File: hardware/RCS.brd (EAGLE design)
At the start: 47 x 40.5 mm, 60 parts, among them U1 LT1930, U2 TD62083AFNG, U3 HX711, U4 HX711

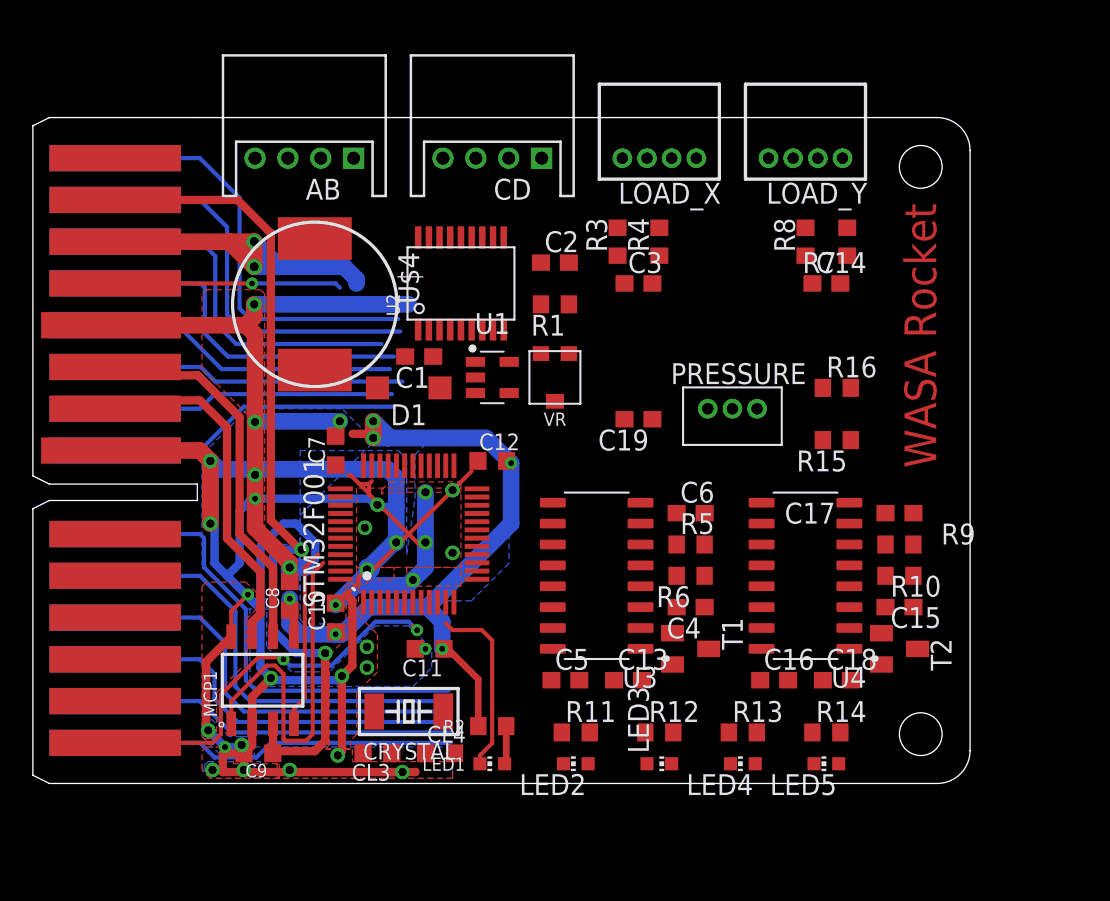
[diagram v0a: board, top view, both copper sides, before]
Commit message: RCS基板を追加
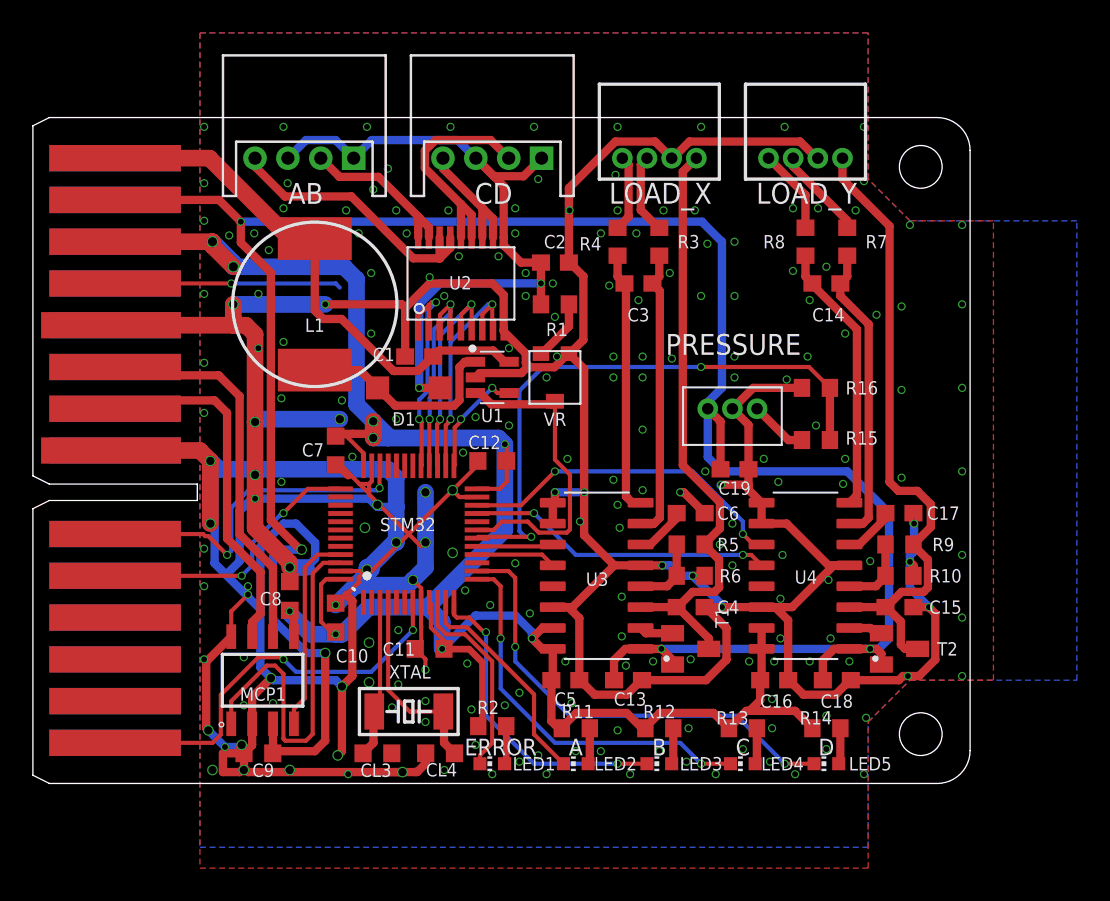
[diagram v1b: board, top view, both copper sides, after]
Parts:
- moved C19 6.59 mm to (42.7, 19.2), turned to 0 degrees
- moved R3 2.54 mm to (38.1, 33.0)
- moved R4 2.54 mm to (35.6, 33.0)
- moved R15 1.27 mm to (47.6, 21.0)
- moved R16 1.27 mm to (47.6, 24.1)
- moved R11 0.25 mm to (33.0, 3.43)
- moved R12 0.25 mm to (38.1, 3.43)
- moved R13 0.25 mm to (43.2, 3.43)
- moved R14 0.25 mm to (48.3, 3.43)
- turned C12 to 180 degrees
- turned C15 to 0 degrees
- turned C4 to 0 degrees
- turned C7 to 270 degrees
- turned LED3 to 90 degrees
- renumbered CRYSTAL to XTAL, STM32F001 to STM32, U$4 to L1
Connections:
- net N$10 renamed D_OUT
- net N$12 renamed A_OUT
- net N$8 renamed B_OUT
- net N$9 renamed C_OUT
- removed net N$24: U$2.30
- removed net N$28: STM32.10
- removed net N$33: U$2.29
- removed net N$34: U$2.28
- removed net N$35: U$2.27
- removed net N$36: U$2.26
- removed net N$43: U$2.25
- removed net N$44: U$2.23
- removed net N$45: U$2.22
- removed net N$46: U$2.21
- removed net N$47: U$2.20
- removed net N$48: U$2.19
- removed net N$49: U$2.18
- removed net N$72: U$2.16
- removed net N$73: U$2.17
- net N$51: now also STM32.10
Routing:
- net GND: track 188.9 -> 363.4 mm, vias 32 -> 217
- net VCC: track 51.1 -> 143.0 mm, vias 2 -> 5
- net VDD: track 68.9 -> 128.7 mm, vias 8 -> 9
- net V_VALVE: track 0.00 -> 43.7 mm, vias 0 -> 2
- net Y_VDD: track 0.00 -> 38.9 mm
- net X_VDD: track 0.00 -> 36.7 mm
- net PRESSURE: track 0.00 -> 35.9 mm, vias 0 -> 2
- net VPP: track 0.00 -> 32.7 mm
- net N$25: track 0.00 -> 28.3 mm, vias 0 -> 2
- net N$43: track 27.8 -> 0.00 mm
- net N$36: track 26.1 -> 0.00 mm
- net N$72: track 25.2 -> 0.00 mm
- net N$35: track 24.6 -> 0.00 mm
- net N$73: track 23.8 -> 0.00 mm
- net N$22: track 0.00 -> 23.7 mm, vias 0 -> 2
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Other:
- board text added: "A"
- board text added: "A+ A- B+ B-"
- board text added: "B"
- board text added: "C"
- board text added: "C+ C- D+ D-"
- board text added: "D"
- board text added: "ERROR"
- board text added: "RCS Module"
- board text added: "V G + -"
- board text removed: "WASA Rocket Project"

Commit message: 気圧センサ用ポートを追加
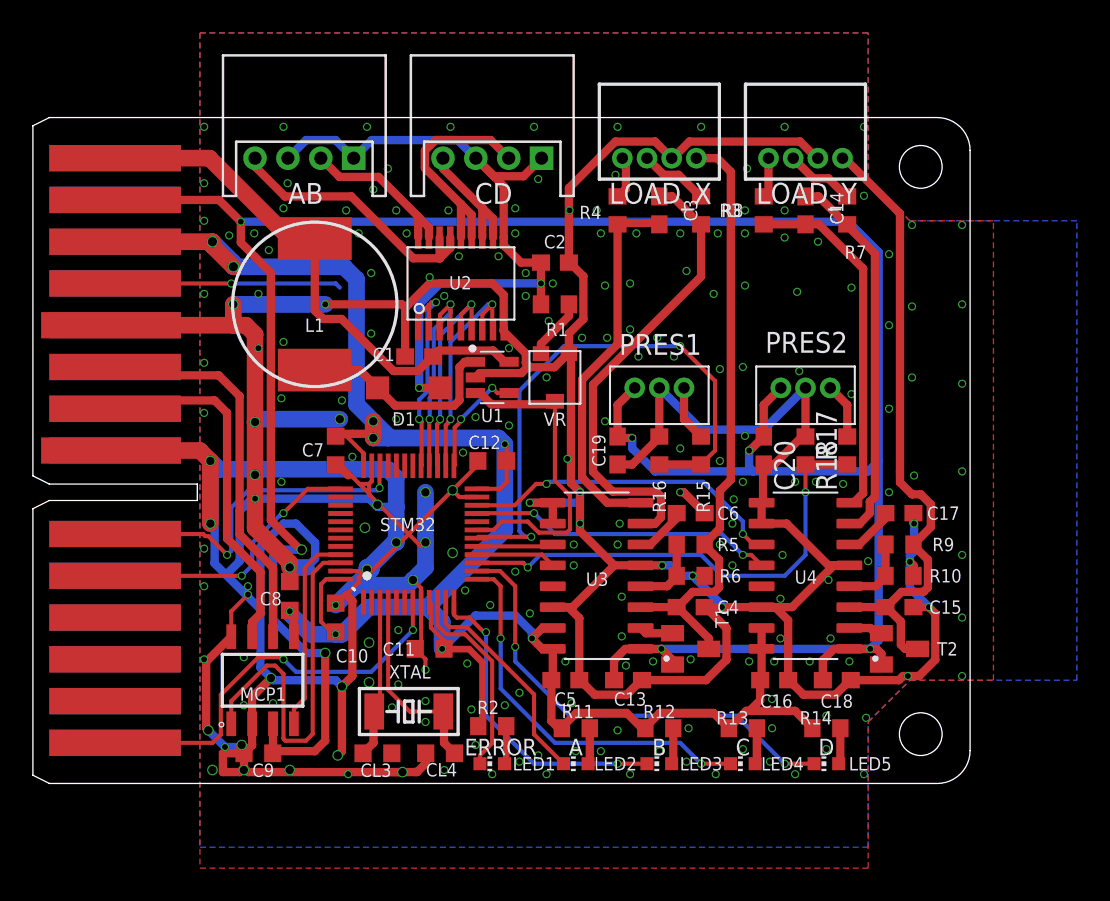
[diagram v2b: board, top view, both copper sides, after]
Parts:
- removed PRESSURE: B3B-ZR, jst:B3B-ZR
- added C20: (no value), rcl:C0603
- added PRES1, PRES2: B3B-ZR, jst:B3B-ZR
- added R17: 10k, rcl:R0603
- added R18: 15k, rcl:R0603
- moved R16 10.3 mm to (38.1, 20.3), turned to 270 degrees
- moved C19 7.20 mm to (35.6, 20.3), turned to 270 degrees
- moved R15 7.01 mm to (40.6, 20.3), turned to 90 degrees
- moved C3 4.62 mm to (38.1, 34.9), turned to 90 degrees
- moved C14 4.62 mm to (47.0, 34.9), turned to 90 degrees
- moved R3 3.17 mm to (40.6, 34.9)
- moved R8 3.17 mm to (44.5, 34.9)
- moved R4 1.90 mm to (35.6, 34.9)
- moved R7 1.90 mm to (49.5, 34.9)
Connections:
- net PRESSURE renamed PRESSURE_1
- new net N$8: PRES2.3, R17.2
- new net PRESSURE_2: R17.1, R18.2, STM32.15
- net GND: now also C20.2, PRES1.2, PRES2.2, R18.1; no longer PRESSURE.2
- net N$17: now also PRES1.3; no longer PRESSURE.3
- net VCC: now also C20.1, PRES1.1, PRES2.1; no longer PRESSURE.1
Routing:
- net PRESSURE_2: track 0.00 -> 29.5 mm, vias 0 -> 2
- net VCC: track 143.0 -> 165.0 mm, vias 5 -> 7
- net GND: track 363.4 -> 378.8 mm, vias 217 -> 221
- net N$3: track 17.6 -> 28.5 mm
- net N$4: track 15.9 -> 23.1 mm
- net N$13: track 16.5 -> 21.9 mm
- net N$11: track 18.1 -> 23.2 mm
- net N$8: track 0.00 -> 3.39 mm
- net Y_SIG+: track 5.16 -> 2.45 mm
- net X_SIG+: track 4.67 -> 2.65 mm
- net Y_SIG-: track 5.59 -> 4.25 mm
- net PRESSURE_1: track 35.9 -> 34.6 mm
- net X_VDD: track 36.7 -> 37.3 mm
- net X_SIG-: track 4.89 -> 4.30 mm
- net Y_SCK: track 20.5 -> 19.9 mm
